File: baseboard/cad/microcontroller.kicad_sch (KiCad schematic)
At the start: 10 parts, among them J16 Conn_01x04_Pin, K1 TQ2-L2-3V3, K2 TQ2-L2-3V3, U10 STM32L011F3Ux, U11 DRV8212P, U12 DRV8212P, Y1 830054236

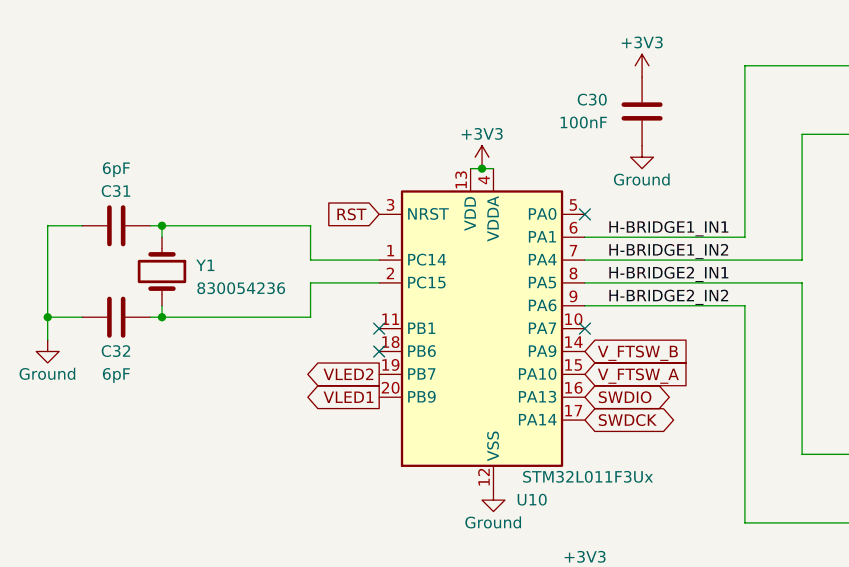
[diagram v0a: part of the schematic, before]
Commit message: added microcontroller enable to analog power rails
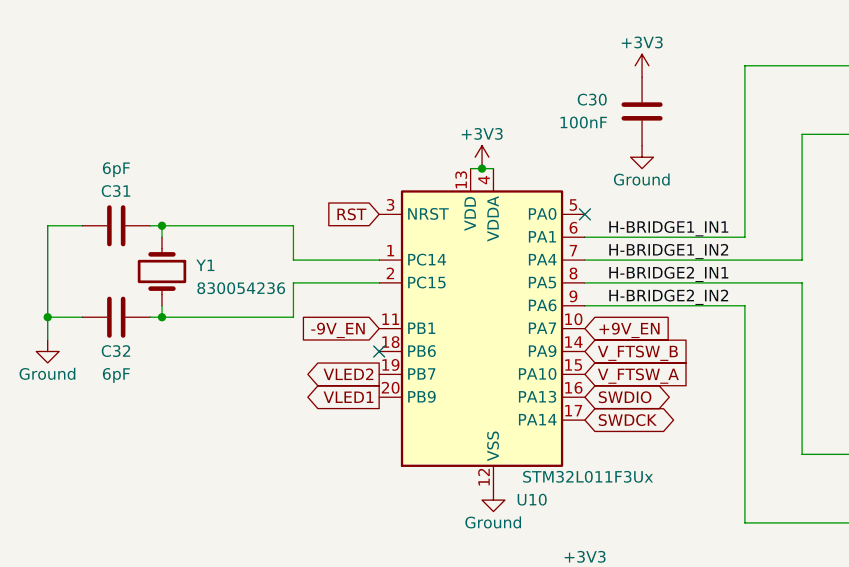
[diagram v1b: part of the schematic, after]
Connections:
- net +9V_EN: now reaches U10.10 (PA7)
- net -9V_EN: now reaches U10.11 (PB1)
- no-connect marks 4 -> 2
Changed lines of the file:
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@@
   (junction (at 68.58 92.71) (diameter 0) (color 0 0 0 0)
   )
-  (no_connect (at 115.57 93.98))
   (no_connect (at 115.57 81.28))
-  (no_connect (at 92.71 93.98))
   (no_connect (at 92.71 96.52))
   (wire (pts (xy 205.74 87.63) (xy 190.5 87.63))
@@
     (stroke (width 0) (type default))
   )
-  (wire (pts (xy 85.09 88.9) (xy 92.71 88.9))
-    (stroke (width 0) (type default))
-  )
-  (wire (pts (xy 85.09 86.36) (xy 92.71 86.36))
+  (wire (pts (xy 83.185 88.9) (xy 92.71 88.9))
+    (stroke (width 0) (type default))
+  )
+  (wire (pts (xy 83.185 86.36) (xy 92.71 86.36))
     (stroke (width 0) (type default))
   )
@@
     (stroke (width 0) (type default))
   )
-  (wire (pts (xy 68.58 82.55) (xy 85.09 82.55))
+  (wire (pts (xy 68.58 82.55) (xy 83.185 82.55))
     (stroke (width 0) (type default))
   )
@@
     (stroke (width 0) (type default))
   )
-  (wire (pts (xy 85.09 82.55) (xy 85.09 86.36))
+  (wire (pts (xy 83.185 82.55) (xy 83.185 86.36))
     (stroke (width 0) (type default))
   )
@@
     (stroke (width 0) (type default))
   )
-  (wire (pts (xy 68.58 92.71) (xy 85.09 92.71))
+  (wire (pts (xy 68.58 92.71) (xy 83.185 92.71))
     (stroke (width 0) (type default))
   )
@@
     (stroke (width 0) (type default))
   )
-  (wire (pts (xy 85.09 92.71) (xy 85.09 88.9))
+  (wire (pts (xy 83.185 92.71) (xy 83.185 88.9))
     (stroke (width 0) (type default))
   )
@@
     (stroke (width 0) (type default))
   )
-  (image (at 173.99 151.13) (scale 1.864)
+  (image (at 201.295 173.355) (scale 1.864)
     (data
       iVBORw0KGgoAAAANSUhEUgAAAwAAAACbCAYAAADVyPyTAAAABHNCSVQICAgIfAhkiAAAAAlwSFlz
@@
     )
   )
+  (global_label "-9V_EN" (shape input) (at 92.71 93.98 180) (fields_autoplaced)
+    (effects (font (size 1.27 1.27)) (justify right))
+    (property "Intersheetrefs" "${INTERSHEET_REFS}" (at 83.5524 93.98 0)
+      (effects (font (size 1.27 1.27)) (justify right) hide)
+    )
+  )
   (global_label "VLED2" (shape output) (at 92.71 99.06 180) (fields_autoplaced)
     (effects (font (size 1.27 1.27)) (justify right))
@@
       (effects (font (size 1.27 1.27)) (justify left) hide)
     )
+  )
+  (global_label "+9V_EN" (shape input) (at 115.57 93.98 0) (fields_autoplaced)
+    (effects (font (size 1.27 1.27)) (justify left))
+    (property "Intersheetrefs" "${INTERSHEET_REFS}" (at 124.7276 93.98 0)
+      (effects (font (size 1.27 1.27)) (justify left) hide)
+    )

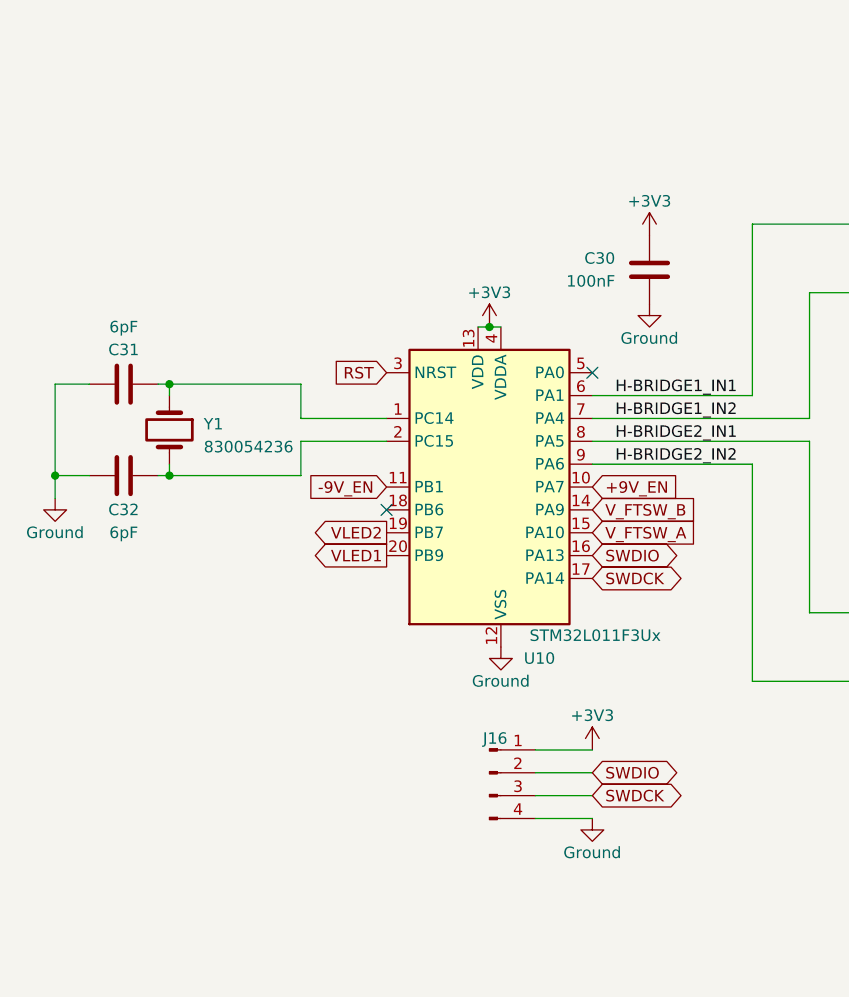
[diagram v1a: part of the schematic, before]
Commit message: added reset button to microcontroller
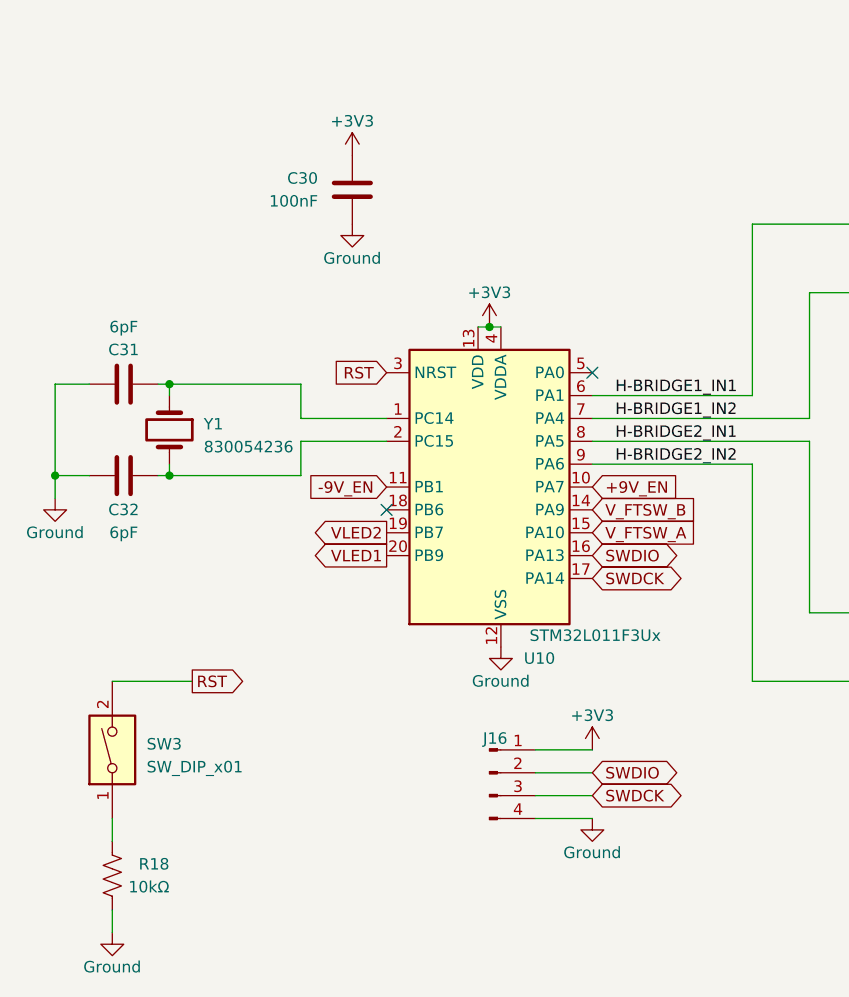
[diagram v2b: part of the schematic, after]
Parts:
- added R18: 10kΩ, Resistor_SMD:R_0603_1608Metric, symbol Device:R_US
- added SW3: SW_DIP_x01, symbol Switch:SW_DIP_x01
- Y1: footprint (none) -> Crystal:Crystal_SMD_3215-2Pin_3.2x1.5mm
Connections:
- net GND: now also R18.2
- net RST: now also SW3.2
- new net: R18.1, SW3.1
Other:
- moved on the sheet: C30
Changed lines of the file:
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@@
+    (stroke (width 0) (type default))
+  )
+  (wire (pts (xy 62.23 130.81) (xy 62.23 133.35))
     (stroke (width 0) (type default))
   )
@@
     (stroke (width 0) (type default))
   )
+  (wire (pts (xy 71.12 115.57) (xy 62.23 115.57))
+    (stroke (width 0) (type default))
+  )
   (wire (pts (xy 190.5 69.85) (xy 190.5 62.23))
     (stroke (width 0) (type default))
@@
   )
   (wire (pts (xy 59.69 82.55) (xy 55.88 82.55))
+    (stroke (width 0) (type default))
+  )
+  (wire (pts (xy 62.23 140.97) (xy 62.23 143.51))
     (stroke (width 0) (type default))
   )
@@
     )
   )
-  (symbol (lib_id "Library:Ground") (at 121.92 73.66 0) (unit 1)
-    (in_bom yes) (on_board yes) (dnp no)
-    (property "Reference" "#PWR039" (at 121.92 80.01 0)
-      (effects (font (size 1.27 1.27)) hide)
-    )
-    (property "Value" "Ground" (at 121.92 77.47 0)
-      (effects (font (size 1.27 1.27)))
-    )
-    (property "Footprint" "" (at 121.92 73.66 0)
-      (effects (font (size 1.27 1.27)) hide)
-    )
-    (property "Datasheet" "" (at 121.92 73.66 0)
+  (global_label "RST" (shape output) (at 71.12 115.57 0) (fields_autoplaced)
+    (effects (font (size 1.27 1.27)) (justify left))
+    (property "Intersheetrefs" "${INTERSHEET_REFS}" (at 77.0802 115.57 0)
+      (effects (font (size 1.27 1.27)) (justify left) hide)
+    )
+  )
+  (symbol (lib_id "Library:Ground") (at 88.9 64.77 0) (unit 1)
+    (in_bom yes) (on_board yes) (dnp no)
+    (property "Reference" "#PWR039" (at 88.9 71.12 0)
+      (effects (font (size 1.27 1.27)) hide)
+    )
+    (property "Value" "Ground" (at 88.9 68.58 0)
+      (effects (font (size 1.27 1.27)))
+    )
+    (property "Footprint" "" (at 88.9 64.77 0)
+      (effects (font (size 1.27 1.27)) hide)
+    )
+    (property "Datasheet" "" (at 88.9 64.77 0)
       (effects (font (size 1.27 1.27)) hide)
     )
@@
       (effects (font (size 1.27 1.27)) (justify left))
     )
-    (property "Footprint" "" (at 68.58 87.63 0)
+    (property "Footprint" "Crystal:Crystal_SMD_3215-2Pin_3.2x1.5mm" (at 68.58 87.63 0)
       (effects (font (size 1.27 1.27)) hide)
     )
@@
         (path "/190888c1-6ce2-4681-a836-dc477e444e49/229a97b2-4425-47f7-b588-f32dc6b9bc79"
           (reference "Y1") (unit 1)
+        )
+      )
+    )
+  )
+  (symbol (lib_id "Device:R_US") (at 62.23 137.16 0) (unit 1)
+    (in_bom yes) (on_board yes) (dnp no)
+    (property "Reference" "R18" (at 68.58 135.89 0)
+      (effects (font (size 1.27 1.27)) (justify right))
+    )
+    (property "Value" "10kΩ" (at 68.58 138.43 0)
+      (effects (font (size 1.27 1.27)) (justify right))
+    )
+    (property "Footprint" "Resistor_SMD:R_0603_1608Metric" (at 63.246 137.414 90)
+      (effects (font (size 1.27 1.27)) hide)
+    )
+    (property "Datasheet" "https://www.koaspeer.com/products/resistors/thin-film/rn73h/" (at 62.23 137.16 0)
+      (effects (font (size 1.27 1.27)) hide)
+    )
+    (property "Manufacturer" "Koa Speer" (at 62.23 137.16 0)
+      (effects (font (size 1.27 1.27)) hide)
+    )
+    (property "Part Number" "RN73H1JTTD1002F100" (at 62.23 137.16 0)
+      (effects (font (size 1.27 1.27)) hide)
+    )
+    (pin "1")
+    (pin "2")
+    (instances
+      (project "1590N1 IO Board"
+        (path "/190888c1-6ce2-4681-a836-dc477e444e49/a050f331-207a-415a-9776-ea47c7d16f9f"
+          (reference "R18") (unit 1)
+        )
+        (path "/190888c1-6ce2-4681-a836-dc477e444e49/229a97b2-4425-47f7-b588-f32dc6b9bc79"
+          (reference "R22") (unit 1)
         )
       )
@@
     )
   )
-  (symbol (lib_id "power:+3V3") (at 121.92 66.04 0) (unit 1)
+  (symbol (lib_id "power:+3V3") (at 88.9 57.15 0) (unit 1)
     (in_bom yes) (on_board yes) (dnp no) (fields_autoplaced)
-    (property "Reference" "#PWR012" (at 121.92 69.85 0)
-      (effects (font (size 1.27 1.27)) hide)
-    )
-    (property "Value" "+3V3" (at 121.92 62.23 0)
-      (effects (font (size 1.27 1.27)))
-    )
-    (property "Footprint" "" (at 121.92 66.04 0)
-      (effects (font (size 1.27 1.27)) hide)
-    )
-    (property "Datasheet" "" (at 121.92 66.04 0)
+    (property "Reference" "#PWR012" (at 88.9 60.96 0)
+      (effects (font (size 1.27 1.27)) hide)
+    )
+    (property "Value" "+3V3" (at 88.9 53.34 0)
+      (effects (font (size 1.27 1.27)))
+    )
+    (property "Footprint" "" (at 88.9 57.15 0)
+      (effects (font (size 1.27 1.27)) hide)
+    )
+    (property "Datasheet" "" (at 88.9 57.15 0)
       (effects (font (size 1.27 1.27)) hide)
     )
@@
     )
   )
+  (symbol (lib_id "Switch:SW_DIP_x01") (at 62.23 123.19 90) (unit 1)
+    (in_bom yes) (on_board yes) (dnp no) (fields_autoplaced)
+    (property "Reference" "SW3" (at 66.04 122.555 90)
+      (effects (font (size 1.27 1.27)) (justify right))
+    )
+    (property "Value" "SW_DIP_x01" (at 66.04 125.095 90)
+      (effects (font (size 1.27 1.27)) (justify right))
+    )
+    (property "Footprint" "" (at 62.23 123.19 0)
+      (effects (font (size 1.27 1.27)) hide)
+    )
+    (property "Datasheet" "~" (at 62.23 123.19 0)
+      (effects (font (size 1.27 1.27)) hide)
+    )
+    (pin "1")
+    (pin "2")
+    (instances
+      (project "1590N1 IO Board"
+        (path "/190888c1-6ce2-4681-a836-dc477e444e49/229a97b2-4425-47f7-b588-f32dc6b9bc79"
+          (reference "SW3") (unit 1)
+        )
+      )
+    )
+  )
   (symbol (lib_id "power:+3V3") (at 170.18 90.17 0) (unit 1)
     (in_bom yes) (on_board yes) (dnp no) (fields_autoplaced)
@@
         (path "/190888c1-6ce2-4681-a836-dc477e444e49/229a97b2-4425-47f7-b588-f32dc6b9bc79"
           (reference "#PWR047") (unit 1)
+        )
+      )
+    )
+  )
+  (symbol (lib_id "Library:Ground") (at 62.23 143.51 0) (unit 1)
+    (in_bom yes) (on_board yes) (dnp no)
+    (property "Reference" "#PWR035" (at 62.23 149.86 0)
+      (effects (font (size 1.27 1.27)) hide)
+    )
+    (property "Value" "Ground" (at 62.23 147.32 0)
+      (effects (font (size 1.27 1.27)))
+    )
+    (property "Footprint" "" (at 62.23 143.51 0)
+      (effects (font (size 1.27 1.27)) hide)
+    )
+    (property "Datasheet" "" (at 62.23 143.51 0)
+      (effects (font (size 1.27 1.27)) hide)
+    )
+    (pin "1")
+    (instances
+      (project "1590N1 IO Board"
+        (path "/190888c1-6ce2-4681-a836-dc477e444e49/a050f331-207a-415a-9776-ea47c7d16f9f"
+          (reference "#PWR035") (unit 1)
+        )
+        (path "/190888c1-6ce2-4681-a836-dc477e444e49/229a97b2-4425-47f7-b588-f32dc6b9bc79"
+          (reference "#PWR041") (unit 1)
         )
       )
@@
     )
   )
-  (symbol (lib_id "Device:C") (at 121.92 69.85 180) (unit 1)
-    (in_bom yes) (on_board yes) (dnp no)
-    (property "Reference" "C30" (at 118.11 68.58 0)
+  (symbol (lib_id "Device:C") (at 88.9 60.96 180) (unit 1)
+    (in_bom yes) (on_board yes) (dnp no)
+    (property "Reference" "C30" (at 85.09 59.69 0)
       (effects (font (size 1.27 1.27)) (justify left))
     )
-    (property "Value" "100nF" (at 118.11 71.12 0)
+    (property "Value" "100nF" (at 85.09 62.23 0)
       (effects (font (size 1.27 1.27)) (justify left))
     )
-    (property "Footprint" "Capacitor_SMD:C_1206_3216Metric" (at 120.9548 66.04 0)
-      (effects (font (size 1.27 1.27)) hide)
-    )
-    (property "Datasheet" "https://www.murata.com/en-us/products/capacitor/ceramiccapacitor/overview/lineup/smd/grm#anchor-2" (at 121.92 69.85 0)
-      (effects (font (size 1.27 1.27)) hide)
-    )
-    (property "Manufacturer" "Murata" (at 121.92 69.85 0)
-      (effects (font (size 1.27 1.27)) hide)
-    )
-    (property "Part Number" "GRM31C5C1H104JA01K" (at 121.92 69.85 0)
-      (effects (font (size 1.27 1.27)) hide)
-    )
+    (property "Footprint" "Capacitor_SMD:C_1206_3216Metric" (at 87.9348 57.15 0)
+      (effects (font (size 1.27 1.27)) hide)
+    )
+    (property "Datasheet" "https://www.murata.com/en-us/products/capacitor/ceramiccapacitor/overview/lineup/smd/grm#anchor-2" (at 88.9 60.96 0)
+      (effects (font (size 1.27 1.27)) hide)
+    )
+    (property "Manufacturer" "Murata" (at 88.9 60.96 0)
+      (effects (font (size 1.27 1.27)) hide)
+    )
+    (property "Part Number" "GRM31C5C1H104JA01K" (at 88.9 60.96 0)
+      (effects (font (size 1.27 1.27)) hide)
+    )
